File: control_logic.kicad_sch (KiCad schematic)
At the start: 45 parts, among them SW1 KMR721NGLFS, SW2 KMR721NGLFS, U12 STM32F105RCTx, Y3 8MHz 12pF

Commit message: added todos
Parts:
- removed D20: yellow, LED_SMD:LED_0603_1608Metric, symbol Device:LED_Small
- removed D21: green, LED_SMD:LED_0603_1608Metric, symbol Device:LED_Small
- removed D22: red, LED_SMD:LED_0603_1608Metric, symbol Device:LED_Small
- removed R39: 4k7, Resistor_SMD:R_0402_1005Metric, symbol Device:R_Small
- removed R40, R42: 10k, Resistor_SMD:R_0402_1005Metric, symbol Device:R_Small
- removed R64, R69, R70: 10k, Resistor_SMD:R_0603_1608Metric, symbol Device:R_Small
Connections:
- net CE renamed CE_N
- net FAULT: no longer names the net of U12.27 (PB1)
- net FLIP: no longer names the net of U12.26 (PB0)
- net GPIO_1: no longer names the net of U12.28 (PB2)
- net PG: no longer names the net of U12.36 (PB15)
- net STAT1: no longer names the net of U12.38 (PC7)
- net STAT2: no longer names the net of U12.37 (PC6)
- no-connect marks 20 -> 24
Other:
- note added: "todo: add can bootloader (AN3154)"
- moved on the sheet: R72

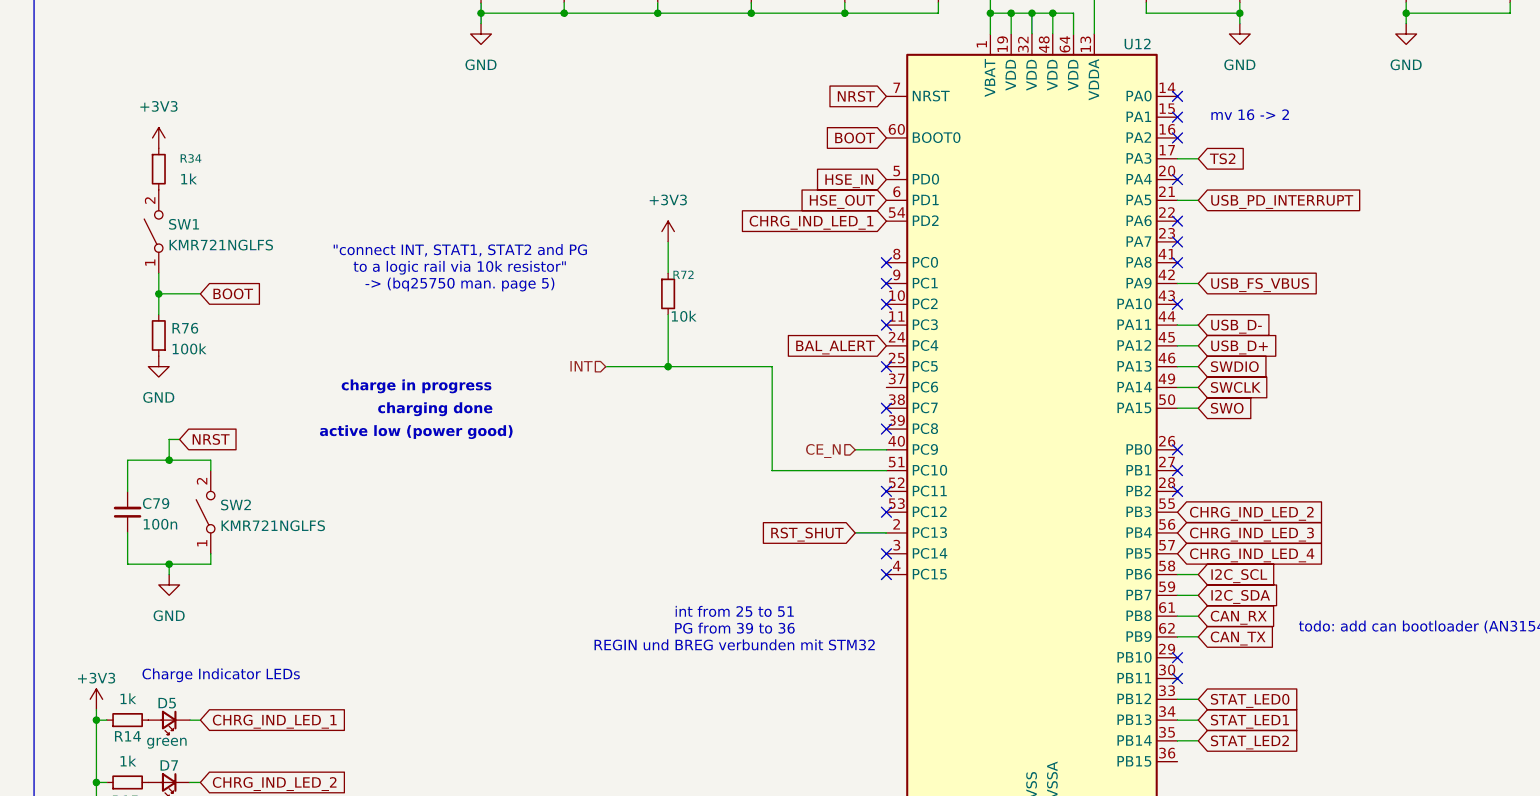
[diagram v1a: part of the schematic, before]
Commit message: added hierarchical pins for submodules
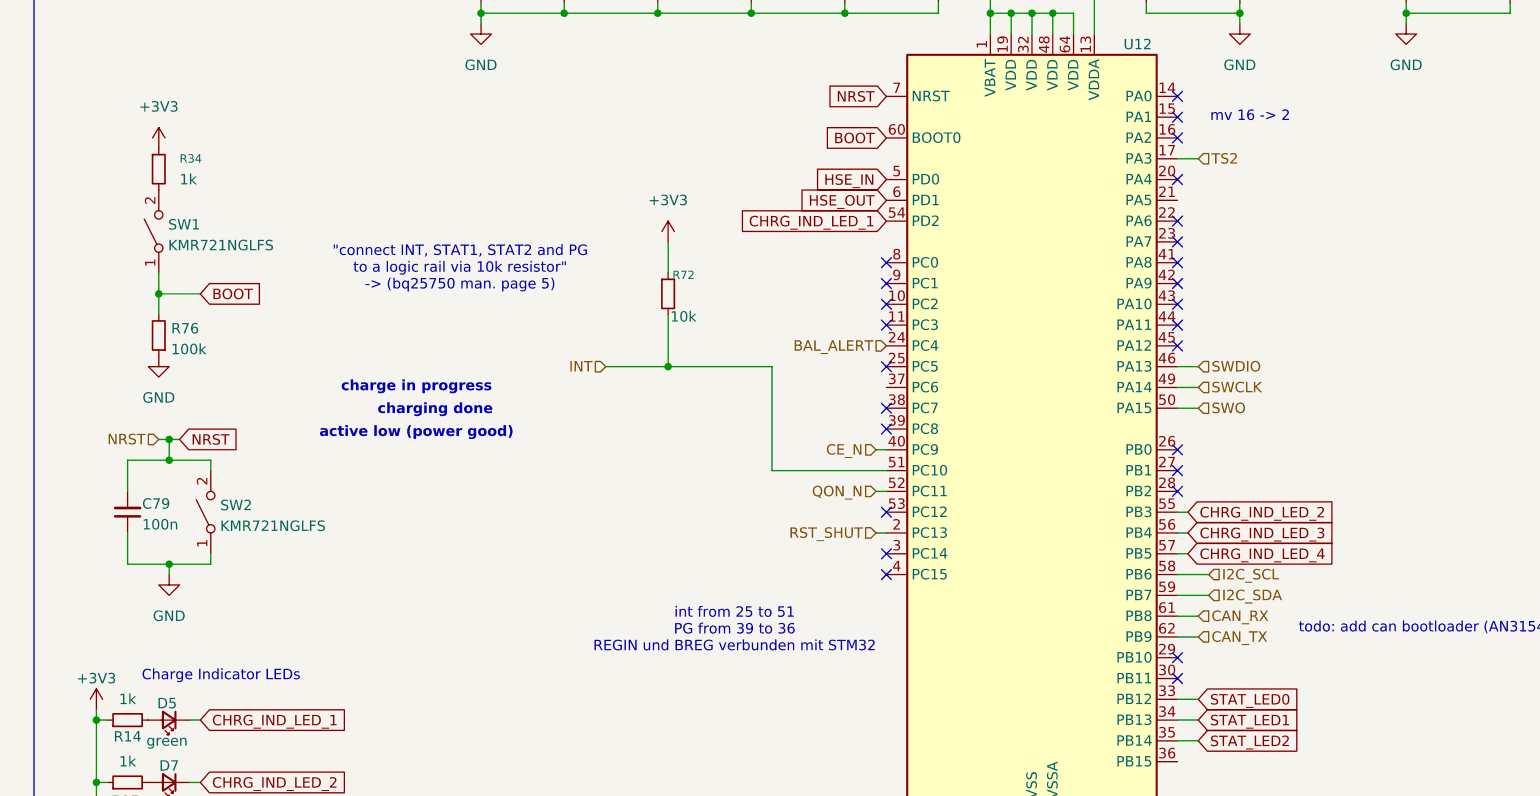
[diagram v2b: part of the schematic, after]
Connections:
- net QON_N: now reaches U12.52 (PC11)
- net USB_D+: no longer names the net of U12.45 (PA12)
- net USB_D-: no longer names the net of U12.44 (PA11)
- net USB_FS_VBUS: no longer names the net of U12.42 (PA9)
- net USB_PD_INTERRUPT: no longer names the net of U12.21 (PA5)
- no-connect marks 24 -> 26

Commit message: added second i2c bus; cleaned up sub-schematic-structure
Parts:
- added C58: 470n, Capacitor_SMD:C_0603_1608Metric, symbol Device:C_Small
- added C60, C63: 100n, Capacitor_SMD:C_0402_1005Metric, symbol Device:C_Small
- added C61: 10u, Capacitor_SMD:C_1206_3216Metric, symbol Device:C_Small
- added C80: 22u, Capacitor_SMD:C_1206_3216Metric, symbol Device:C_Small
- added FB3: 120R, Inductor_SMD:L_0805_2012Metric, symbol Device:FerriteBead
- added J1, J3: Conn_02x04_Top_Bottom, Connector_Molex:Molex_Micro-Fit_3.0_43045-0800_2x04_P3.00mm_Horizontal, symbol Connector_Generic:Conn_02x04_Top_Bottom
- added J12: SWD Header, Connector_PinHeader_2.54mm:PinHeader_1x04_P2.54mm_Vertical_SMD_Pin1Left, symbol Connector_Generic:Conn_01x04
- added J17: TC2050, Connector:Tag-Connect_TC2050-IDC-FP_2x05_P1.27mm_Vertical, symbol Connector_Generic:Conn_02x05_Counter_Clockwise
- added R35: 120, Capacitor_SMD:C_0402_1005Metric, symbol Device:R_Small
- added R66, R67: 4.7k, Resistor_SMD:R_0402_1005Metric, symbol Device:R
- added R77, R78: 22R, Resistor_SMD:R_0402_1005Metric, symbol Device:R_Small
- added R86, R87, R88, R92: 22, Resistor_SMD:R_0402_1005Metric, symbol Device:R_Small
- added U10: L7805, Package_TO_SOT_SMD:TO-252-2, symbol Regulator_Linear:L7805
- added U11: MCP2562-E-SN, Package_SO:SOIC-8_3.9x4.9mm_P1.27mm, symbol Interface_CAN_LIN:MCP2562-E-SN
- added U13: AZ1117I-3.3, Package_TO_SOT_SMD:SOT-223-3_TabPin2, symbol Regulator_Linear:AZ1117-3.3
- added U15: TPD4E1U06, Package_TO_SOT_SMD:SOT-563, symbol stigma:TPD4E001DRL
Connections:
- net +3V3: now also C80.2, J12.1 (Pin_1), J17.7 (Pin_7), J17.8 (Pin_8), R66.2, R67.2, U11.5 (Vio), U13.2 (VO), U15.5 (IO4)
- net CAN_RX: now also U11.4 (RXD)
- net CAN_TX: now also U11.1 (TXD)
- net GND: now also C58.1, C60.2, C61.1, C63.1, C80.1, J1.1 (Pin_1), J1.2 (Pin_2), J12.4 (Pin_4), J17.3 (Pin_3), J17.4 (Pin_4), J3.1 (Pin_1), J3.2 (Pin_2), U10.2 (GND), U11.2 (VSS), U11.8 (STBY), U13.1 (GND), U15.3 (GND)
- net NRST: now also R92.1
- net SWCLK: now also R88.2
- net SWDIO: now also R86.1
- net SWO: now also R87.1
- net I2C2_SCL: now reaches U12.29 (PB10)
- net I2C2_SDA: now reaches U12.30 (PB11)
- net I2C_SCL renamed I2C1_SCL
- net I2C1_SCL: now also R67.1, R78.1
- net I2C_SDA renamed I2C1_SDA
- net I2C1_SDA: now also R66.1, R77.1
- new net: C58.2, FB3.1, U10.1 (IN)
- new net: J12.3 (Pin_3), R77.2
- new net: J12.2 (Pin_2), R78.2
- new net: J1.4 (Pin_4), J3.4 (Pin_4)
- new net: J1.8 (Pin_8), J3.8 (Pin_8)
- new net: J17.1 (Pin_1), R92.2
- new net +5V: C60.1, C61.2, C63.2, J17.10 (Pin_10), J17.9 (Pin_9), U10.3 (OUT), U11.3 (VDD), U13.3 (VI), U15.6 (V_{cc})
- new net CAN+: J1.7 (Pin_7), J3.7 (Pin_7), R35.1, U11.7 (CANH)
- new net CAN-: J1.3 (Pin_3), J3.3 (Pin_3), R35.2, U11.6 (CANL)
- new net J1-SWCLK: J17.6 (Pin_6), R88.1, U15.4 (IO3)
- new net J1-SWDIO: J17.2 (Pin_2), R86.2, U15.1 (IO1)
- new net J1-SWO: J17.5 (Pin_5), R87.2, U15.2 (IO2)
- new net SYS+: FB3.2
- new net charging_voltage: J1.5 (Pin_5), J3.5 (Pin_5)
- new net main_voltage: J1.6 (Pin_6), J3.6 (Pin_6)
- no-connect marks 26 -> 24
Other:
- note added: "CAN"
- note added: "Clock"
- note added: "DNP"
- note added: "INFO: it SEEMS like the only outside-connection for voltage is SYS+ (and maybe GND). but 5v, 3v3 and 3va3 are only used by the MCU -> made only SYS+ hierarchical. Please check, if this makes sense"
- note added: "LEDs"
- note added: "Regulators"
- note added: "Vehicle BUS"
- note added: "can2 optional, not neccesary on this board"
- note added: "programming adapters"
- note added: "todo: -connect to vehicle bus and charge voltage -add diodes"
- note added: "todo: -ensure 5v -why are we connecting 3v3 and not nrst? -add a second i2c-swd-header (one for charger, one for balancer) -shouldnt we also protect BOOT?"
- note added: "todo: -is charging_voltage really output? -is main_voltage really output? -is ts2 input or output? -is bal_alert input or output? -is qon_n input or output? -is rst_shut input or output? -is int input or output?"
- note added: "todo: add can bootloader"
- moved on the sheet: C67, C68, C69, C70, C71, C72, C73, C74, C75, C76, C77, C78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

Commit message: Cleaned up, added some Balancer designs
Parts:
- removed C58: 470n, Capacitor_SMD:C_0603_1608Metric, symbol Device:C_Small
- removed C60: 100n, Capacitor_SMD:C_0402_1005Metric, symbol Device:C_Small
- removed C61: 10u, Capacitor_SMD:C_1206_3216Metric, symbol Device:C_Small
- removed C80: 22u, Capacitor_SMD:C_1206_3216Metric, symbol Device:C_Small
- removed FB3: 120R, Inductor_SMD:L_0805_2012Metric, symbol Device:FerriteBead
- removed J1, J3: Conn_02x04_Top_Bottom, Connector_Molex:Molex_Micro-Fit_3.0_43045-0800_2x04_P3.00mm_Horizontal, symbol Connector_Generic:Conn_02x04_Top_Bottom
- removed U10: L7805, Package_TO_SOT_SMD:TO-252-2, symbol Regulator_Linear:L7805
- removed U13: AZ1117I-3.3, Package_TO_SOT_SMD:SOT-223-3_TabPin2, symbol Regulator_Linear:AZ1117-3.3
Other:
- note removed: "INFO: it SEEMS like the only outside-connection for voltage is SYS+ (and maybe GND). but 5v, 3v3 and 3va3 are only used by the MCU -> made only SYS+ hierarchical. Please check, if this makes sense"
- note removed: "Regulators"
- note removed: "Vehicle BUS"
- note removed: "can2 optional, not neccesary on this board"
- note removed: "todo: -connect to vehicle bus and charge voltage -add diodes"

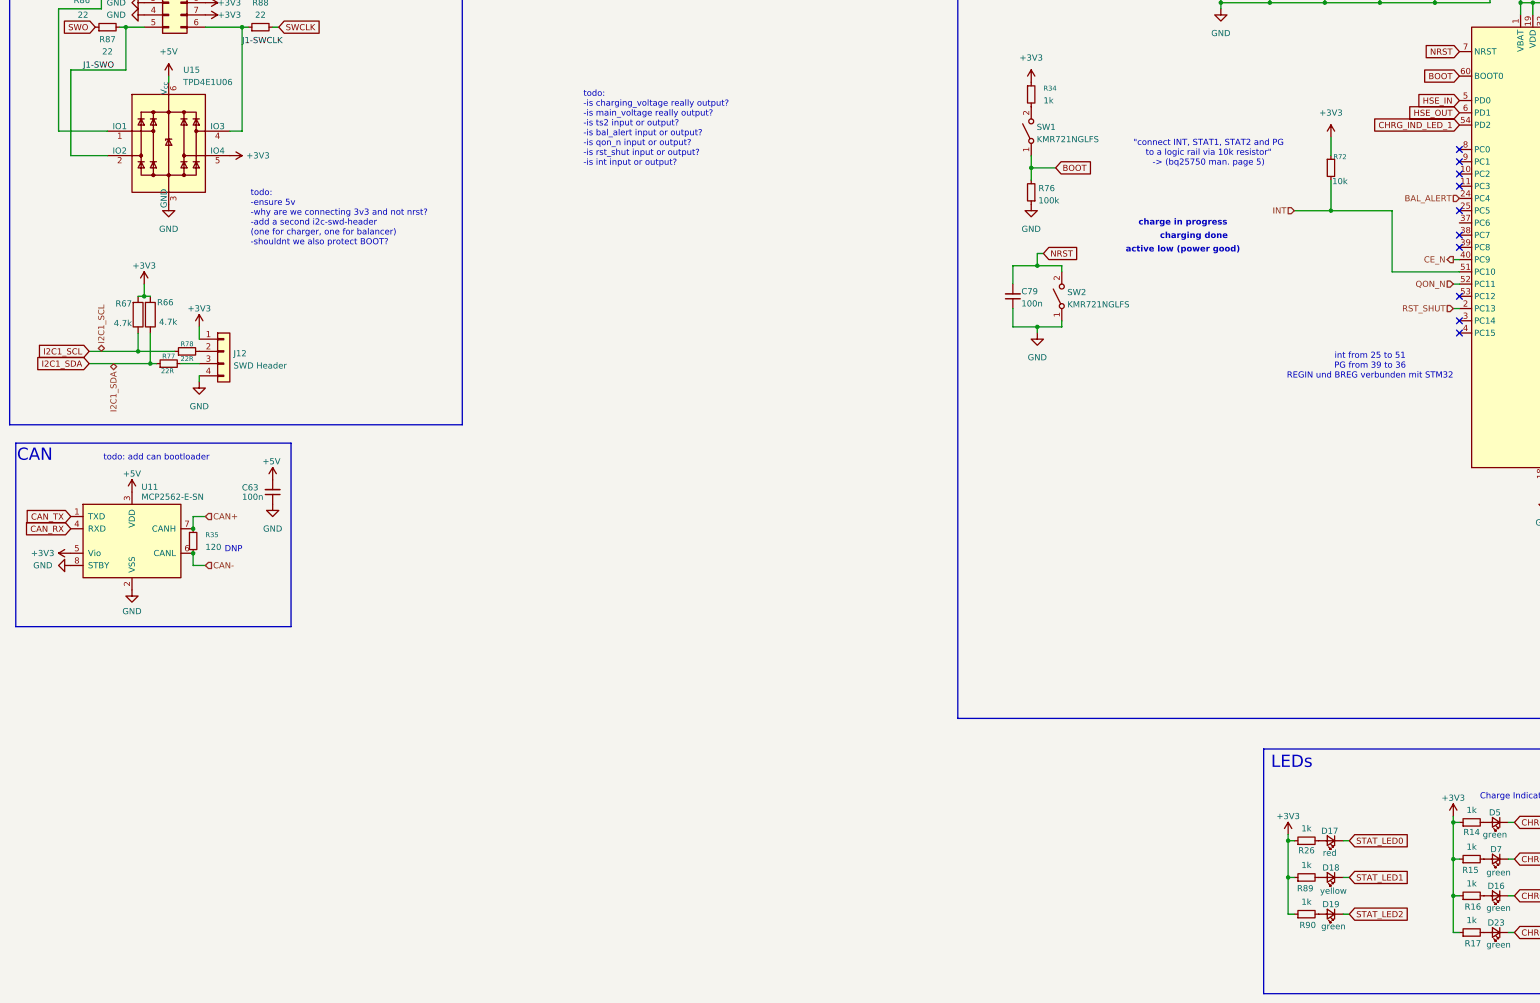
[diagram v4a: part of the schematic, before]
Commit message: cleaned up hierarchical structure; changed connectors
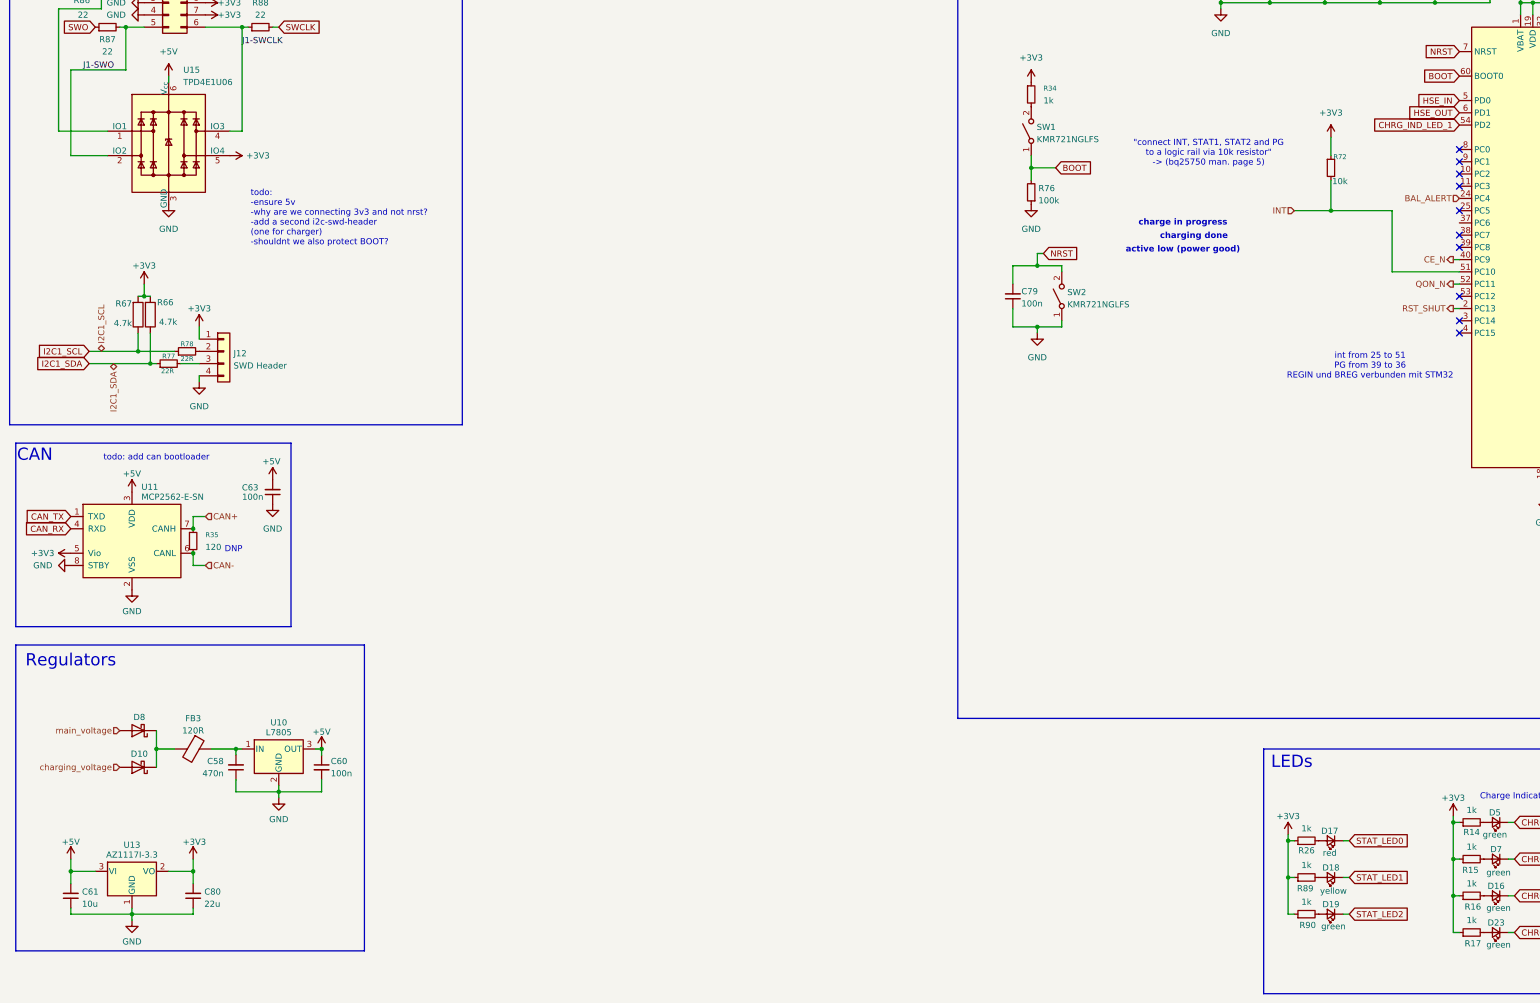
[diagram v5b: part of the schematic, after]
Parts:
- added C58: 470n, Capacitor_SMD:C_0603_1608Metric, symbol Device:C_Small
- added C60: 100n, Capacitor_SMD:C_0402_1005Metric, symbol Device:C_Small
- added C61: 10u, Capacitor_SMD:C_1206_3216Metric, symbol Device:C_Small
- added C80: 22u, Capacitor_SMD:C_1206_3216Metric, symbol Device:C_Small
- added D10, D8: ~, Diode_SMD:D_SMA, symbol Device:D_Schottky
- added FB3: 120R, Inductor_SMD:L_0805_2012Metric, symbol Device:FerriteBead
- added U10: L7805, Package_TO_SOT_SMD:TO-252-2, symbol Regulator_Linear:L7805
- added U13: AZ1117I-3.3, Package_TO_SOT_SMD:SOT-223-3_TabPin2, symbol Regulator_Linear:AZ1117-3.3
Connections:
- net +3V3: now also C80.2, U13.2 (VO)
- net +5V: now also C60.1, C61.2, U10.3 (OUT), U13.3 (VI)
- net GND: now also C58.1, C60.2, C61.1, C80.1, U10.2 (GND), U13.1 (GND)
- new net: C58.2, FB3.1, U10.1 (IN)
- new net: D10.1 (K), D8.1 (K), FB3.2
- new net charging_voltage: D10.2 (A)
- new net main_voltage: D8.2 (A)
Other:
- note added: "Regulators"
- note added: "todo: -ensure 5v -why are we connecting 3v3 and not nrst? -add a second i2c-swd-header (one for charger) -shouldnt we also protect BOOT?"
- note removed: "todo: -ensure 5v -why are we connecting 3v3 and not nrst? -add a second i2c-swd-header (one for charger, one for balancer) -shouldnt we also protect BOOT?"
- note removed: "todo: -is charging_voltage really output? -is main_voltage really output? -is ts2 input or output? -is bal_alert input or output? -is qon_n input or output? -is rst_shut input or output? -is int input or output?"
